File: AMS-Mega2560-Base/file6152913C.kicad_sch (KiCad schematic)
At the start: 11 parts, among them IC16 DS3231SN#, IC17 MAX232CPE+, J33 Conn_01x02, U3 S8411-45R

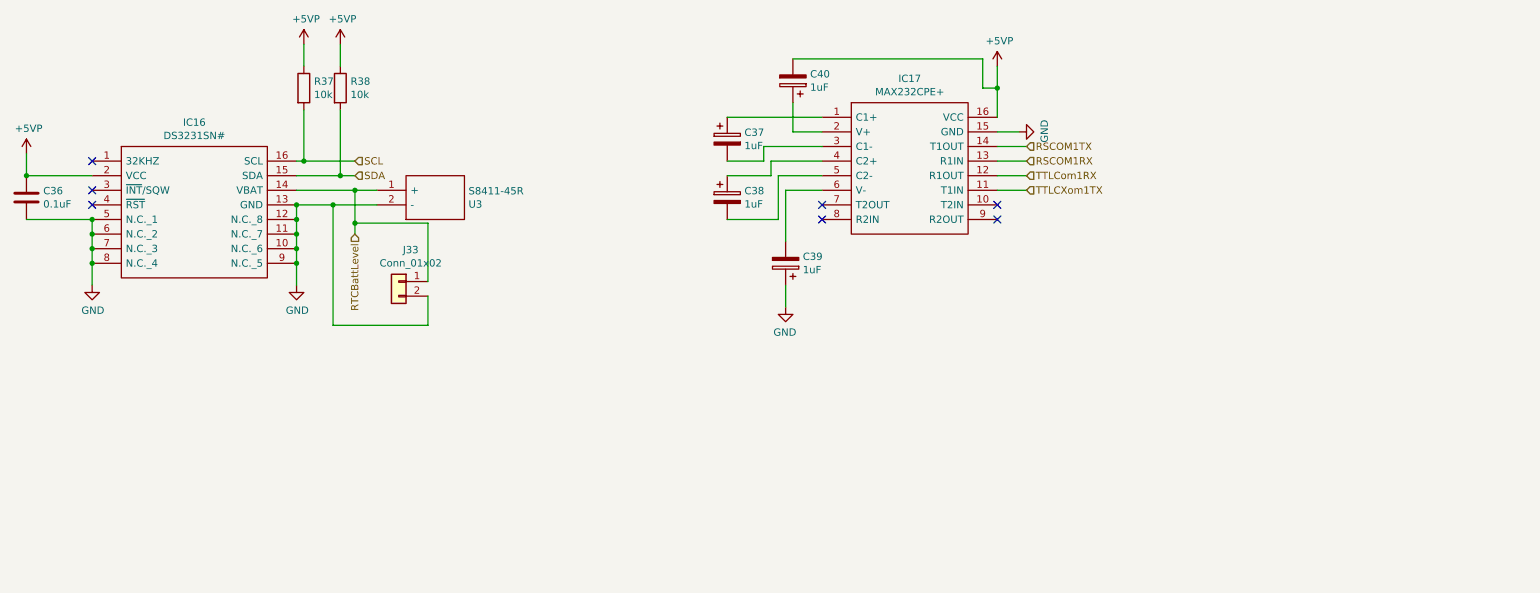
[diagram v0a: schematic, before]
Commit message: WIP for power on input and RTC battery switch over.
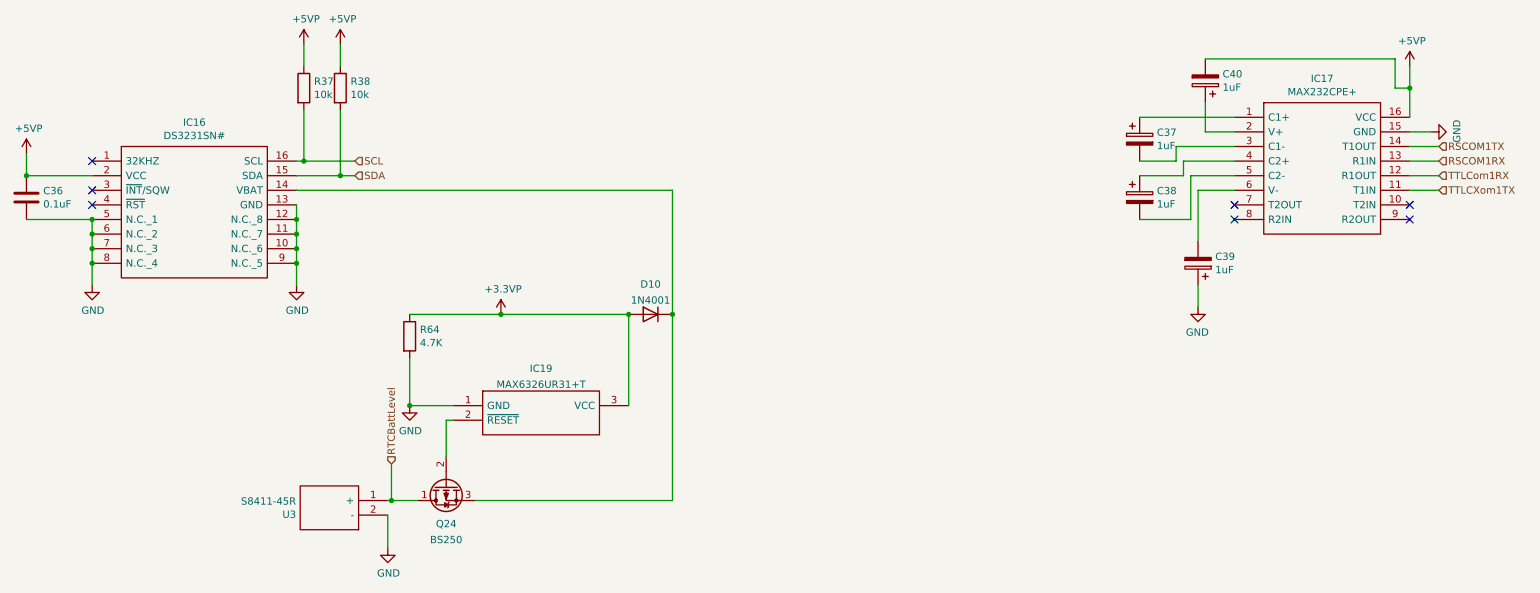
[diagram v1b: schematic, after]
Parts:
- removed J33: Conn_01x02, Connector_PinHeader_2.54mm:PinHeader_1x02_P2.54mm_Vertical, symbol Connector_Generic:Conn_01x02
- added D10: 1N4001, Diode_THT:D_DO-41_SOD81_P10.16mm_Horizontal, symbol Diode:1N4001
- added IC19: MAX6326UR31+T, SOT95P237X112-3N, symbol Samac_Sys:MAX6326UR31+T
- added Q24: BS250, Package_TO_SOT_THT:TO-92_Inline, symbol Transistor_FET:BS250
- added R64: 4.7K, Resistor_THT:R_Axial_DIN0207_L6.3mm_D2.5mm_P2.54mm_Vertical, symbol Device:R
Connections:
- net GND: now also IC19.1 (GND), R64.2
- net RTCBattLevel: now also Q24.1 (D); no longer IC16.14 (VBAT)
- new net: D10.1 (K), IC16.14 (VBAT), Q24.3 (S)
- new net: IC19.2 (~{RESET}), Q24.2 (G)
- new net +3.3VP: D10.2 (A), IC19.3 (VCC), R64.1
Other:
- moved on the sheet: C37, C38, C39, C40, IC17, U3

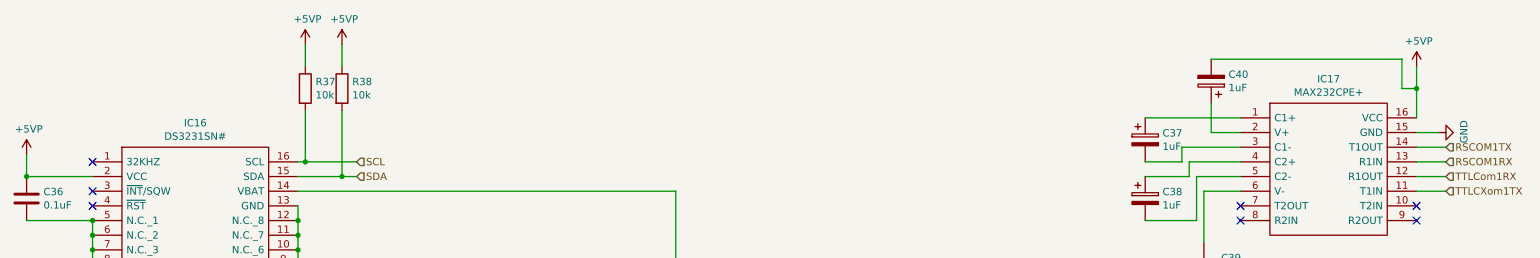
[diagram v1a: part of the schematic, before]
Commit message: fixing the 5V lines and removing the 5V fromt he MCU board and only using the 3Amp 5v power supplied by CampKeen
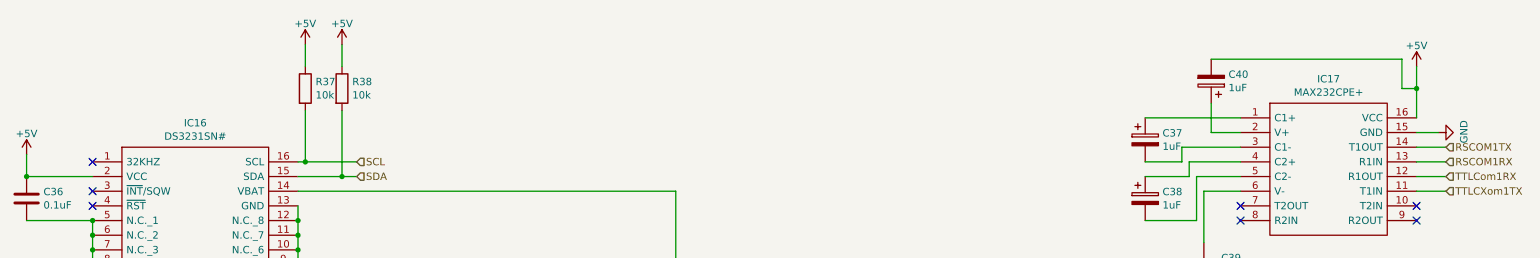
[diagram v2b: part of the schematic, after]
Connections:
- net +5VP renamed +5V
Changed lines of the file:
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@@
     (pin "9")
   )
-  (symbol (lib_id "power:+5VP") (at 69.85 20.32 0) (unit 1)
-    (in_bom yes) (on_board yes)
-    (property "Reference" "#PWR0101" (id 0) (at 69.85 24.13 0)
-      (effects (font (size 1.27 1.27)) hide)
-    )
-    (property "Value" "+5VP" (id 1) (at 70.231 15.9258 0))
-    (property "Footprint" "" (id 2) (at 69.85 20.32 0)
-      (effects (font (size 1.27 1.27)) hide)
-    )
-    (property "Datasheet" "" (id 3) (at 69.85 20.32 0)
-      (effects (font (size 1.27 1.27)) hide)
-    )
-    (pin "1")
-  )
   (symbol (lib_id "Device:R") (at 69.85 27.94 0) (unit 1)
     (in_bom yes) (on_board yes)
@@
     (pin "2")
   )
-  (symbol (lib_id "power:+5VP") (at 76.2 20.32 0) (unit 1)
-    (in_bom yes) (on_board yes)
-    (property "Reference" "#PWR0102" (id 0) (at 76.2 24.13 0)
-      (effects (font (size 1.27 1.27)) hide)
-    )
-    (property "Value" "+5VP" (id 1) (at 76.581 15.9258 0))
-    (property "Footprint" "" (id 2) (at 76.2 20.32 0)
-      (effects (font (size 1.27 1.27)) hide)
-    )
-    (property "Datasheet" "" (id 3) (at 76.2 20.32 0)
-      (effects (font (size 1.27 1.27)) hide)
-    )
-    (pin "1")
-  )
   (symbol (lib_id "Device:R") (at 76.2 27.94 0) (unit 1)
     (in_bom yes) (on_board yes)
@@
     (pin "1")
     (pin "2")
-  )
-  (symbol (lib_id "power:+5VP") (at 262.255 24.13 0) (unit 1)
-    (in_bom yes) (on_board yes)
-    (property "Reference" "#PWR0104" (id 0) (at 262.255 27.94 0)
-      (effects (font (size 1.27 1.27)) hide)
-    )
-    (property "Value" "+5VP" (id 1) (at 262.636 19.7358 0))
-    (property "Footprint" "" (id 2) (at 262.255 24.13 0)
-      (effects (font (size 1.27 1.27)) hide)
-    )
-    (property "Datasheet" "" (id 3) (at 262.255 24.13 0)
-      (effects (font (size 1.27 1.27)) hide)
-    )
-    (pin "1")
   )
   (symbol (lib_id "power:GND") (at 68.58 62.23 0) (unit 1)
@@
     (pin "1")
     (pin "2")
-  )
-  (symbol (lib_id "power:+5VP") (at 21.59 39.37 0) (unit 1)
-    (in_bom yes) (on_board yes)
-    (property "Reference" "#PWR098" (id 0) (at 21.59 43.18 0)
-      (effects (font (size 1.27 1.27)) hide)
-    )
-    (property "Value" "+5VP" (id 1) (at 21.971 34.9758 0))
-    (property "Footprint" "" (id 2) (at 21.59 39.37 0)
-      (effects (font (size 1.27 1.27)) hide)
-    )
-    (property "Datasheet" "" (id 3) (at 21.59 39.37 0)
-      (effects (font (size 1.27 1.27)) hide)
-    )
-    (pin "1")
   )
   (symbol (lib_id "Device:C") (at 21.59 46.99 0) (unit 1)
@@
     (pin "1")
   )
+  (symbol (lib_id "power:+5V") (at 262.255 24.13 0) (unit 1)
+    (in_bom yes) (on_board yes) (fields_autoplaced)
+    (property "Reference" "#PWR?" (id 0) (at 262.255 27.94 0)
+      (effects (font (size 1.27 1.27)) hide)
+    )
+    (property "Value" "+5V" (id 1) (at 262.255 20.5255 0))
+    (property "Footprint" "" (id 2) (at 262.255 24.13 0)
+      (effects (font (size 1.27 1.27)) hide)
+    )
+    (property "Datasheet" "" (id 3) (at 262.255 24.13 0)
+      (effects (font (size 1.27 1.27)) hide)
+    )
+    (pin "1")
+  )
+  (symbol (lib_id "power:+5V") (at 21.59 39.37 0) (unit 1)
+    (in_bom yes) (on_board yes) (fields_autoplaced)
+    (property "Reference" "#PWR?" (id 0) (at 21.59 43.18 0)
+      (effects (font (size 1.27 1.27)) hide)
+    )
+    (property "Value" "+5V" (id 1) (at 21.59 35.7655 0))
+    (property "Footprint" "" (id 2) (at 21.59 39.37 0)
+      (effects (font (size 1.27 1.27)) hide)
+    )
+    (property "Datasheet" "" (id 3) (at 21.59 39.37 0)
+      (effects (font (size 1.27 1.27)) hide)
+    )
+    (pin "1")
+  )
   (symbol (lib_id "power:+3.3VP") (at 104.14 67.31 0) (unit 1)
     (in_bom yes) (on_board yes)
@@
     (pin "3")
   )
+  (symbol (lib_id "power:+5V") (at 69.85 20.32 0) (unit 1)
+    (in_bom yes) (on_board yes) (fields_autoplaced)
+    (property "Reference" "#PWR?" (id 0) (at 69.85 24.13 0)
+      (effects (font (size 1.27 1.27)) hide)
+    )
+    (property "Value" "+5V" (id 1) (at 69.85 16.7155 0))
+    (property "Footprint" "" (id 2) (at 69.85 20.32 0)
+      (effects (font (size 1.27 1.27)) hide)
+    )
+    (property "Datasheet" "" (id 3) (at 69.85 20.32 0)
+      (effects (font (size 1.27 1.27)) hide)
+    )
+    (pin "1")
+  )
+  (symbol (lib_id "power:+5V") (at 76.2 20.32 0) (unit 1)
+    (in_bom yes) (on_board yes) (fields_autoplaced)
+    (property "Reference" "#PWR?" (id 0) (at 76.2 24.13 0)
+      (effects (font (size 1.27 1.27)) hide)
+    )
+    (property "Value" "+5V" (id 1) (at 76.2 16.7155 0))
+    (property "Footprint" "" (id 2) (at 76.2 20.32 0)
+      (effects (font (size 1.27 1.27)) hide)
+    )
+    (property "Datasheet" "" (id 3) (at 76.2 20.32 0)
+      (effects (font (size 1.27 1.27)) hide)
+    )
+    (pin "1")
+  )
 )

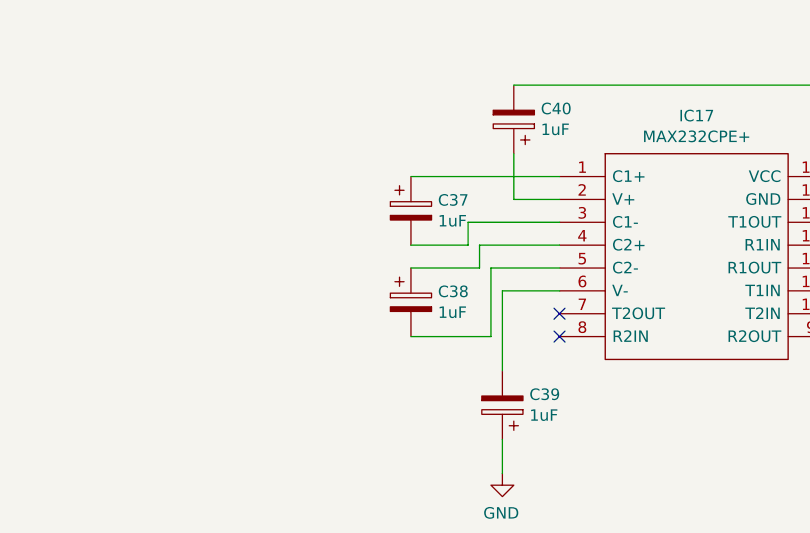
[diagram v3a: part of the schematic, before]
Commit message: cleared all of the ERC stuff need to go over some of the power stuff for this before finishing routing.
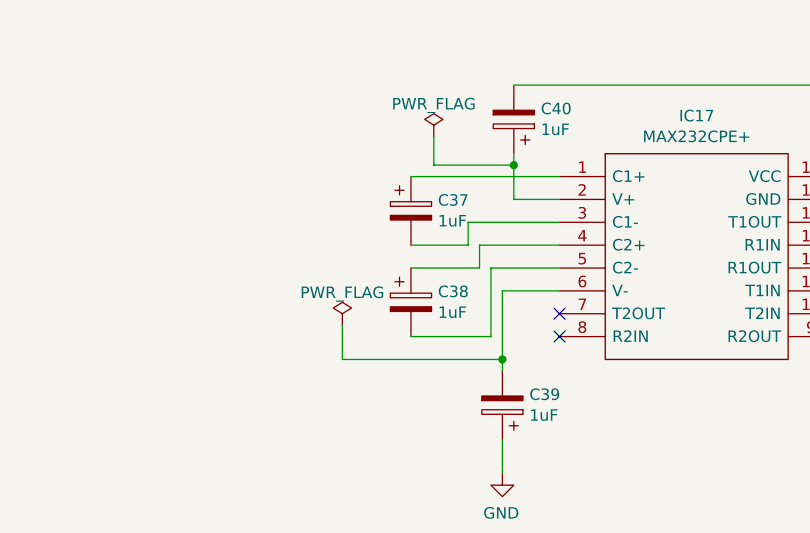
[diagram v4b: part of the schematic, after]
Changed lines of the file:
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@@
   (junction (at 104.14 67.31) (diameter 0) (color 0 0 0 0)
   )
+  (junction (at 226.695 31.75) (diameter 0) (color 0 0 0 0)
+  )
   (junction (at 68.58 50.8) (diameter 0) (color 0 0 0 0)
   )
@@
   )
   (junction (at 76.2 43.18) (diameter 0) (color 0 0 0 0)
+  )
+  (junction (at 225.425 53.34) (diameter 0) (color 0 0 0 0)
   )
   (junction (at 33.02 58.42) (diameter 0) (color 0 0 0 0)
@@
     (stroke (width 0) (type default) (color 0 0 0 0))
   )
-  (wire (pts (xy 226.695 35.56) (xy 226.695 30.48))
+  (wire (pts (xy 226.695 35.56) (xy 226.695 31.75))
     (stroke (width 0) (type default) (color 0 0 0 0))
   )
@@
     (stroke (width 0) (type default) (color 0 0 0 0))
   )
+  (wire (pts (xy 225.425 54.61) (xy 225.425 53.34))
+    (stroke (width 0) (type default) (color 0 0 0 0))
+  )
+  (wire (pts (xy 68.58 50.8) (xy 68.58 48.26))
+    (stroke (width 0) (type default) (color 0 0 0 0))
+  )
+  (wire (pts (xy 207.645 49.53) (xy 207.645 53.34))
+    (stroke (width 0) (type default) (color 0 0 0 0))
+  )
+  (wire (pts (xy 78.74 40.64) (xy 69.85 40.64))
+    (stroke (width 0) (type default) (color 0 0 0 0))
+  )
+  (wire (pts (xy 262.255 43.18) (xy 267.335 43.18))
+    (stroke (width 0) (type default) (color 0 0 0 0))
+  )
+  (wire (pts (xy 84.455 102.235) (xy 84.455 107.95))
+    (stroke (width 0) (type default) (color 0 0 0 0))
+  )
+  (wire (pts (xy 221.615 40.64) (xy 215.265 40.64))
+    (stroke (width 0) (type default) (color 0 0 0 0))
+  )
+  (wire (pts (xy 217.805 28.575) (xy 217.805 31.75))
+    (stroke (width 0) (type default) (color 0 0 0 0))
+  )
+  (wire (pts (xy 222.885 43.18) (xy 222.885 40.64))
+    (stroke (width 0) (type default) (color 0 0 0 0))
+  )
+  (wire (pts (xy 226.695 22.86) (xy 259.715 22.86))
+    (stroke (width 0) (type default) (color 0 0 0 0))
+  )
+  (wire (pts (xy 104.14 67.31) (xy 126.365 67.31))
+    (stroke (width 0) (type default) (color 0 0 0 0))
+  )
+  (wire (pts (xy 69.85 31.75) (xy 69.85 40.64))
+    (stroke (width 0) (type default) (color 0 0 0 0))
+  )
+  (wire (pts (xy 84.455 99.695) (xy 85.09 99.695))
+    (stroke (width 0) (type default) (color 0 0 0 0))
+  )
+  (wire (pts (xy 217.805 31.75) (xy 226.695 31.75))
+    (stroke (width 0) (type default) (color 0 0 0 0))
+  )
   (wire (pts (xy 215.265 50.8) (xy 224.155 50.8))
     (stroke (width 0) (type default) (color 0 0 0 0))
   )
-  (wire (pts (xy 225.425 54.61) (xy 225.425 45.72))
-    (stroke (width 0) (type default) (color 0 0 0 0))
-  )
-  (wire (pts (xy 68.58 50.8) (xy 68.58 48.26))
-    (stroke (width 0) (type default) (color 0 0 0 0))
-  )
-  (wire (pts (xy 78.74 40.64) (xy 69.85 40.64))
-    (stroke (width 0) (type default) (color 0 0 0 0))
-  )
-  (wire (pts (xy 262.255 43.18) (xy 267.335 43.18))
-    (stroke (width 0) (type default) (color 0 0 0 0))
-  )
-  (wire (pts (xy 84.455 102.235) (xy 84.455 107.95))
-    (stroke (width 0) (type default) (color 0 0 0 0))
-  )
-  (wire (pts (xy 221.615 40.64) (xy 215.265 40.64))
-    (stroke (width 0) (type default) (color 0 0 0 0))
-  )
-  (wire (pts (xy 222.885 43.18) (xy 222.885 40.64))
-    (stroke (width 0) (type default) (color 0 0 0 0))
-  )
-  (wire (pts (xy 226.695 22.86) (xy 259.715 22.86))
-    (stroke (width 0) (type default) (color 0 0 0 0))
-  )
-  (wire (pts (xy 104.14 67.31) (xy 126.365 67.31))
-    (stroke (width 0) (type default) (color 0 0 0 0))
-  )
-  (wire (pts (xy 69.85 31.75) (xy 69.85 40.64))
-    (stroke (width 0) (type default) (color 0 0 0 0))
-  )
-  (wire (pts (xy 84.455 99.695) (xy 85.09 99.695))
-    (stroke (width 0) (type default) (color 0 0 0 0))
-  )
   (wire (pts (xy 68.58 45.72) (xy 133.985 45.72))
     (stroke (width 0) (type default) (color 0 0 0 0))
@@
     (stroke (width 0) (type default) (color 0 0 0 0))
   )
+  (wire (pts (xy 207.645 53.34) (xy 225.425 53.34))
+    (stroke (width 0) (type default) (color 0 0 0 0))
+  )
   (wire (pts (xy 78.74 43.18) (xy 76.2 43.18))
     (stroke (width 0) (type default) (color 0 0 0 0))
   )
+  (wire (pts (xy 225.425 53.34) (xy 225.425 45.72))
+    (stroke (width 0) (type default) (color 0 0 0 0))
+  )
   (wire (pts (xy 68.58 58.42) (xy 68.58 55.88))
     (stroke (width 0) (type default) (color 0 0 0 0))
@@
   )
   (wire (pts (xy 259.715 22.86) (xy 259.715 27.94))
+    (stroke (width 0) (type default) (color 0 0 0 0))
+  )
+  (wire (pts (xy 226.695 31.75) (xy 226.695 30.48))
     (stroke (width 0) (type default) (color 0 0 0 0))
   )
@@
     (pin "1")
   )
+  (symbol (lib_id "power:PWR_FLAG") (at 207.645 49.53 0) (unit 1)
+    (in_bom yes) (on_board yes) (fields_autoplaced)
+    (property "Reference" "#FLG0105" (id 0) (at 207.645 47.625 0)
+      (effects (font (size 1.27 1.27)) hide)
+    )
+    (property "Value" "PWR_FLAG" (id 1) (at 207.645 45.9255 0))
+    (property "Footprint" "" (id 2) (at 207.645 49.53 0)
+      (effects (font (size 1.27 1.27)) hide)
+    )
+    (property "Datasheet" "~" (id 3) (at 207.645 49.53 0)
+      (effects (font (size 1.27 1.27)) hide)
+    )
+    (pin "1")
+  )
   (symbol (lib_id "power:+5V") (at 262.255 24.13 0) (unit 1)
     (in_bom yes) (on_board yes) (fields_autoplaced)
@@
       (effects (font (size 1.27 1.27)) hide)
     )
+    (pin "1")
+  )
+  (symbol (lib_id "power:PWR_FLAG") (at 217.805 28.575 0) (unit 1)
+    (in_bom yes) (on_board yes) (fields_autoplaced)
+    (property "Reference" "#FLG0106" (id 0) (at 217.805 26.67 0)
+      (effects (font (size 1.27 1.27)) hide)
+    )
+    (property "Value" "PWR_FLAG" (id 1) (at 217.805 24.9705 0))
+    (property "Footprint" "" (id 2) (at 217.805 28.575 0)
+      (effects (font (size 1.27 1.27)) hide)
+    )
+    (property "Datasheet" "~" (id 3) (at 217.805 28.575 0)
+      (effects (font (size 1.27 1.27)) hide)
+    )
